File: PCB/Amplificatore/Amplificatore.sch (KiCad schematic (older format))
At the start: 75 parts, among them J1 POT-GAIN, J10 POWER, J11 FILAMENT-U2, J12 FILAMENT-U1, J2 POT-LEAD, J3 SEND-RETURN, J4 In, J5 POT-BASS-BACK, J6 POT-MID, J7 POT-TREBLE, J8 POT-BASS-FRONT, J9 MASTER, K1 G5Q-1, K2 G5Q-1, K3 G5Q-1, K4 G5Q-1, U1 ECC83, U2 ECC83

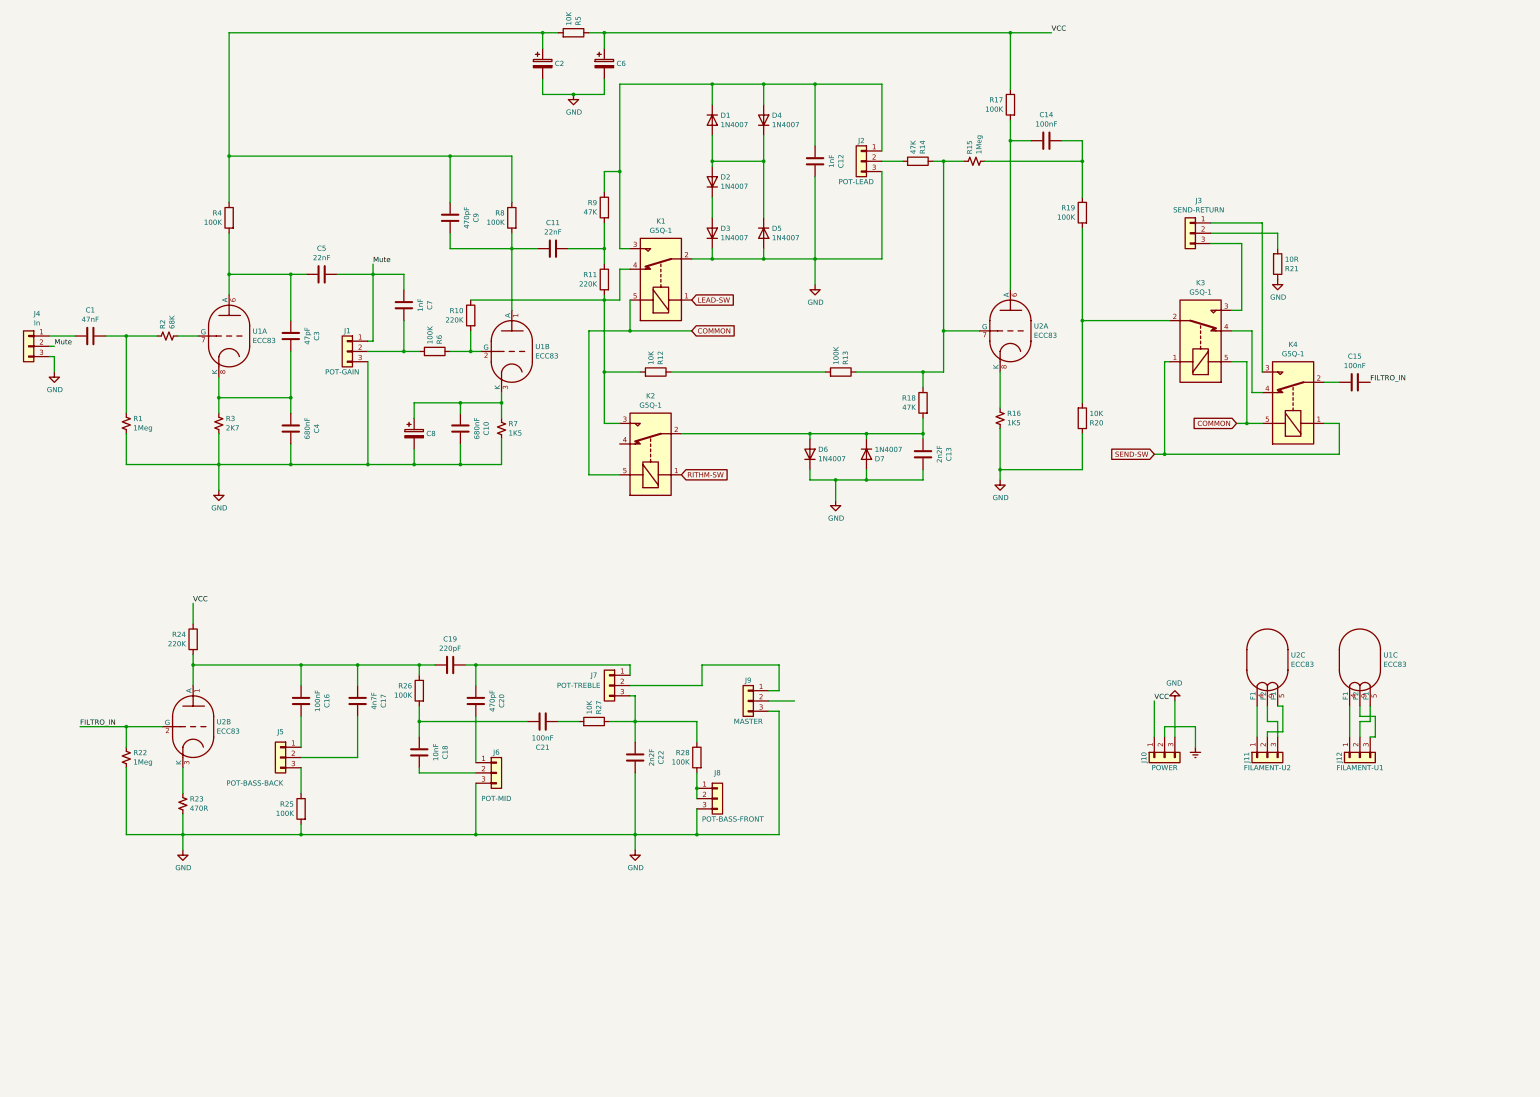
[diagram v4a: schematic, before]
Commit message: sbrogliato pcb pre-ampli
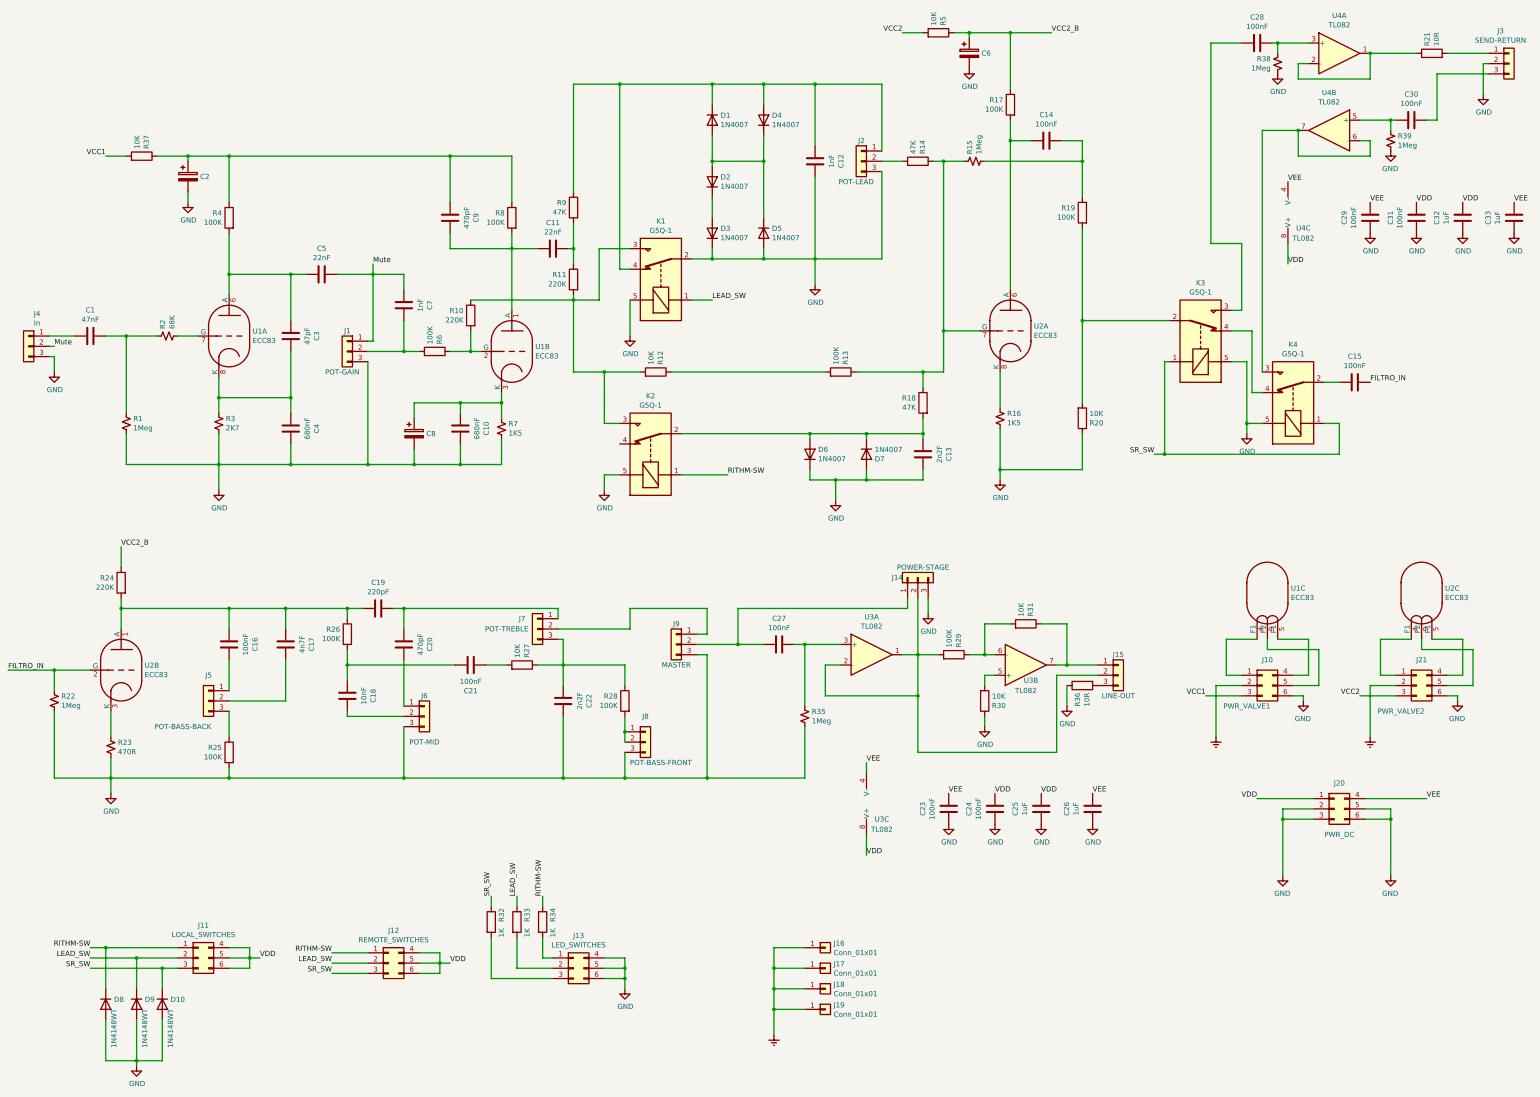
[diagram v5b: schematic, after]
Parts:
- removed J10: POWER, Connector_Molex:Molex_KK-396_A-41791-0003_1x03_P3.96mm_Vertical, symbol Connector_Generic:Conn_01x03
- removed J11: FILAMENT-U2, Connector_PinSocket_2.00mm:PinSocket_1x03_P2.00mm_Vertical, symbol Connector_Generic:Conn_01x03
- removed J12: FILAMENT-U1, Connector_PinSocket_2.00mm:PinSocket_1x03_P2.00mm_Vertical, symbol Connector_Generic:Conn_01x03
- added C23, C24, C29, C31: 100nF, Capacitor_SMD:C_0805_2012Metric_Pad1.18x1.45mm_HandSolder, symbol Device:C
- added C25, C26, C32, C33: 1uF, Capacitor_SMD:C_1206_3216Metric_Pad1.33x1.80mm_HandSolder, symbol Device:C
- added C27, C28, C30: 100nF, Capacitor_THT:C_Rect_L18.0mm_W5.0mm_P15.00mm_FKS3_FKP3, symbol Device:C
- added D10, D8, D9: 1N4148WT, Diode_SMD:D_SOD-523, symbol Diode:1N4148WT
- added J10: PWR_VALVE1, Connector_Molex:Molex_Micro-Fit_3.0_43045-0612_2x03_P3.00mm_Vertical, symbol Connector_Generic:Conn_02x03_Top_Bottom
- added J11: LOCAL_SWITCHES, Connector_Molex:Molex_Micro-Fit_3.0_43045-0612_2x03_P3.00mm_Vertical, symbol Connector_Generic:Conn_02x03_Top_Bottom
- added J12: REMOTE_SWITCHES, Connector_Molex:Molex_Micro-Fit_3.0_43045-0612_2x03_P3.00mm_Vertical, symbol Connector_Generic:Conn_02x03_Top_Bottom
- added J13: LED_SWITCHES, Connector_Molex:Molex_Micro-Fit_3.0_43045-0612_2x03_P3.00mm_Vertical, symbol Connector_Generic:Conn_02x03_Top_Bottom
- added J14: POWER-STAGE, Connector_PinSocket_2.00mm:PinSocket_1x03_P2.00mm_Vertical, symbol Connector_Generic:Conn_01x03
- added J15: LINE-OUT, Connector_PinSocket_2.00mm:PinSocket_1x03_P2.00mm_Vertical, symbol Connector_Generic:Conn_01x03
- added J16, J17, J18, J19: Conn_01x01, MountingHole:MountingHole_3.2mm_M3_DIN965_Pad_TopBottom, symbol Connector_Generic:Conn_01x01
- added J20: PWR_DC, Connector_Molex:Molex_Micro-Fit_3.0_43045-0612_2x03_P3.00mm_Vertical, symbol Connector_Generic:Conn_02x03_Top_Bottom
- added J21: PWR_VALVE2, Connector_Molex:Molex_Micro-Fit_3.0_43045-0612_2x03_P3.00mm_Vertical, symbol Connector_Generic:Conn_02x03_Top_Bottom
- added R29: 100K, Resistor_SMD:R_2512_6332Metric, symbol Device:R
- added R30, R31, R37: 10K, Resistor_SMD:R_2512_6332Metric, symbol Device:R
- added R32, R33, R34: 1K, Resistor_SMD:R_2512_6332Metric, symbol Device:R
- added R35, R38, R39: 1Meg, Resistor_SMD:R_0805_2012Metric, symbol Device:R_Small_US
- added R36: 10R, Resistor_SMD:R_2512_6332Metric, symbol Device:R
- added U3, U4: TL082, Package_SO:SO-8_3.9x4.9mm_P1.27mm, symbol Amplifier_Operational:TL082
- K1, K2, K3, K4: FORNITORE M: 653-G5Q-1DC6 -> M: 653-G5Q-1DC12; PN G5Q-1 DC6 -> G5Q-1-DC12
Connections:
- net COMMON is gone; now on net GND: K1.5, K2.5, K3.5, K4.5
- net Earth: now also J10.2 (Pin_2), J16.1 (Pin_1), J17.1 (Pin_1), J18.1 (Pin_1), J19.1 (Pin_1), J21.2 (Pin_2)
- net GND: now also J3.2 (Pin_2), C23.2, C24.2, C25.2, C26.2, C29.2, C31.2, C32.2, C33.2, D10.2 (A), D8.2 (A), D9.2 (A), J10.6 (Pin_6), J13.4 (Pin_4), J13.5 (Pin_5), J13.6 (Pin_6), J14.3 (Pin_3), J20.2 (Pin_2), J20.3 (Pin_3), J20.5 (Pin_5), J20.6 (Pin_6), J21.6 (Pin_6), R30.1, R35.2, R36.1, R38.2, R39.2; no longer R21.1
- net RITHM-SW: now also D8.1 (K), J11.1 (Pin_1), J12.1 (Pin_1), R34.1
- net at C12.2, D1.1 (K), D4.2 (A)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: now also K1.4; no longer K1.3
- net at K2.3, R10.1, R11.2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: now also K1.3; no longer K1.4
- net at C2.1, C9.2, R4.1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: now also R37.1; no longer R5.2
- net at K3.3: now also C28.2; no longer J3.3 (Pin_3)
- net at J3.1 (Pin_1): now also R21.2; no longer K4.3
- net at J9.2 (Pin_2): now also C27.1, J14.1 (Pin_1)
- net at U1.4 (F1): now also J10.1 (Pin_1)
- net at U1.5 (F1): now also J10.4 (Pin_4)
- net at U1.9 (F2): now also J10.5 (Pin_5)
- net at U2.4 (F1): now also J21.1 (Pin_1)
- net at U2.5 (F1): now also J21.4 (Pin_4)
- net at U2.9 (F2): now also J21.5 (Pin_5)
- net LEAD-SW renamed LEAD_SW
- net LEAD_SW: now also D9.1 (K), J11.2 (Pin_2), J12.2 (Pin_2), R33.1
- net SEND-SW renamed SR_SW
- net SR_SW: now also D10.1 (K), J11.3 (Pin_3), J12.3 (Pin_3), R32.1
- net VCC renamed VCC2_B
- new net: C30.2, J3.3 (Pin_3)
- new net: K4.3, U4.6 (-), U4.7
- new net: R21.1, U4.1, U4.2 (-)
- new net: J14.2 (Pin_2), J15.2 (Pin_2), R29.2, U3.1, U3.2 (-)
- new net: C27.2, R35.1, U3.3 (+)
- new net: R30.2, U3.5 (+)
- new net: R29.1, R31.2, U3.6 (-)
- new net: J15.1 (Pin_1), R31.1, U3.7
- new net: J15.3 (Pin_3), R36.2
- new net: J13.1 (Pin_1), R34.2
- new net: J13.2 (Pin_2), R33.2
- new net: J13.3 (Pin_3), R32.2
- new net: C28.1, R38.1, U4.3 (+)
- new net: C30.1, R39.1, U4.5 (+)
- new net VCC1: J10.3 (Pin_3), R37.2
- new net VCC2: J21.3 (Pin_3), R5.2
- new net VDD: C24.1, C25.1, C31.1, C32.1, J11.4 (Pin_4), J11.5 (Pin_5), J11.6 (Pin_6), J12.4 (Pin_4), J12.5 (Pin_5), J12.6 (Pin_6), J20.1 (Pin_1), U3.8 (V+), U4.8 (V+)
- new net VEE: C23.1, C26.1, C29.1, C33.1, J20.4 (Pin_4), U3.4 (V-), U4.4 (V-)
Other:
- moved on the sheet: C16, C17, C18, C19, C2, C20, C21, C22, C6, J3, J5, J6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
